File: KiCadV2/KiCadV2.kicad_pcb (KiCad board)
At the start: 2 copper layers, 76.4 x 51.6 mm, 148 parts, among them J1 USB_C_Receptacle_PowerOnly_6P, J3 Screw_Terminal_01x02, J4 Screw_Terminal_01x02, U1 MT3608, U10 NC7SZ157P6X, U11 NC7SZ157P6X, U12 NC7SZ157P6X, U13 NC7SZ157P6X, U14 74LV08AT14-13, U15 HIP4080A, U16 NC7SZ157P6X, U17 MX3502S, U18 MX3502S, U2 74HC595, U22 DMHT10H032LFJ, U23 INA240A1D, U26 MX3502S, U3 NC7SZ157P6X, U30 DMHT10H032LFJ, U31 INA240A1D, U32 NC7SZ157P6X, U33 NC7SZ157P6X, U34 NC7SZ157P6X, U35 NC7SZ157P6X, U36 NC7SZ157P6X, U37 NC7SZ157P6X, U38 74LV08AT14-13, U39 HIP4080A, U4 NC7SZ157P6X, U40 MCP6002-xSN, U41 CJ432, U5 MX3502S, U6 NC7SZ157P6X, U7 DAC082S085CISDX/NOPB, U8 NC7SZ157P6X, U9 NC7SZ157P6X

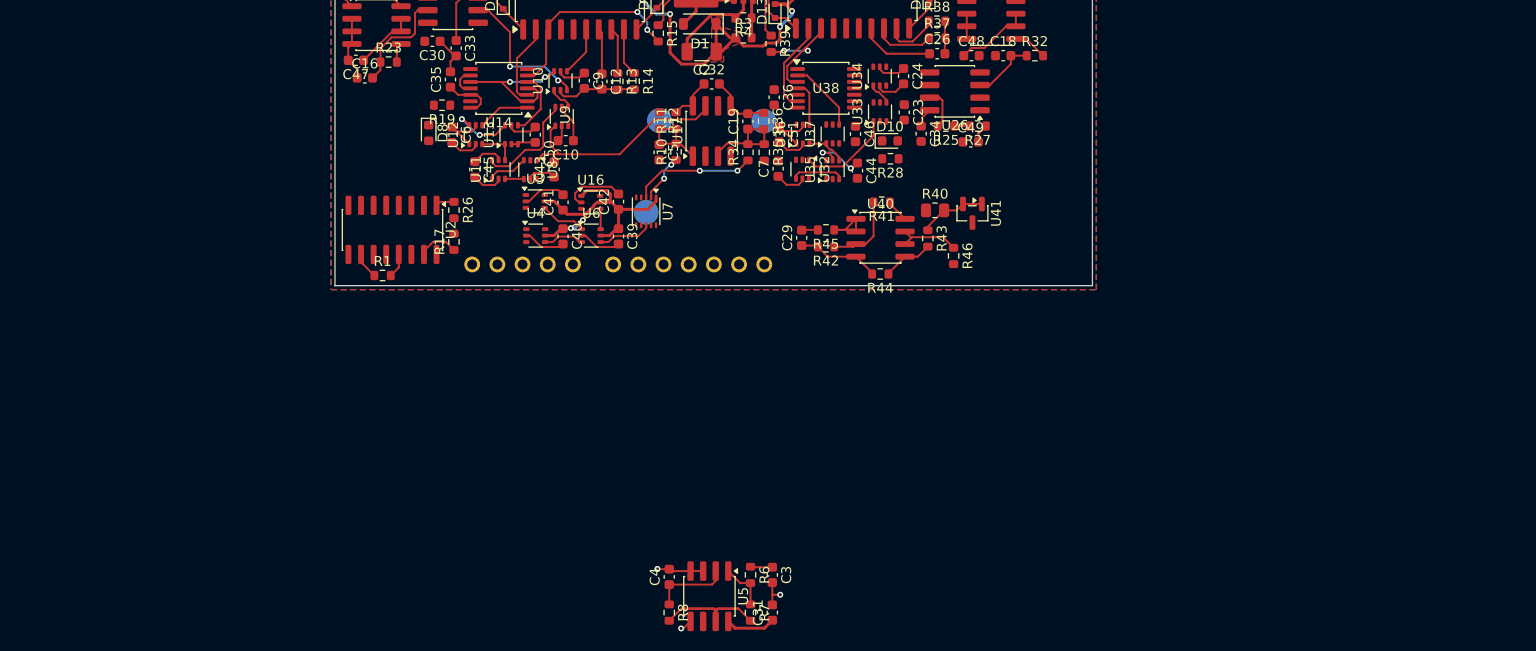
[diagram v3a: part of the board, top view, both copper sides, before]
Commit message: HF PWM done for both coils
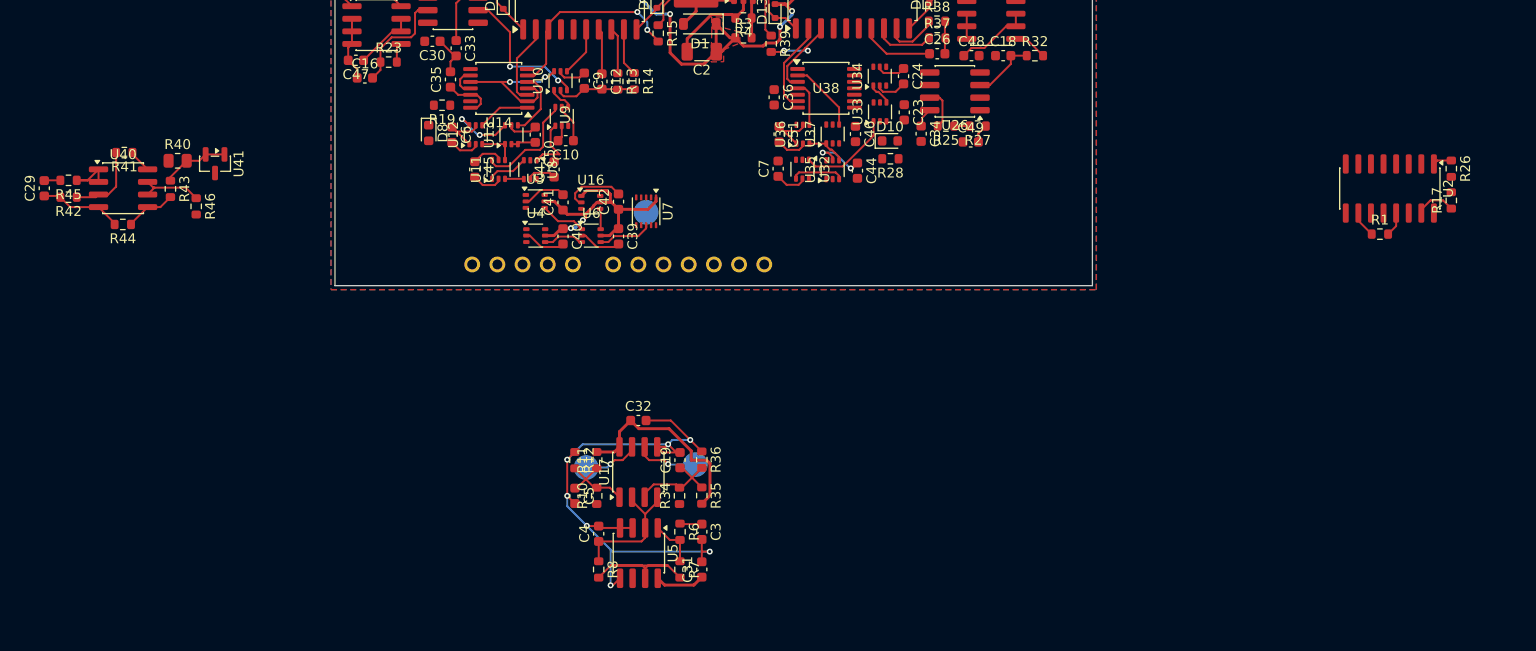
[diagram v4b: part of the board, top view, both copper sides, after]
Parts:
- moved R17 100.7 mm to (170.4, 165.6)
- moved R26 100.7 mm to (170.4, 162.4)
- moved R1 100.7 mm to (163.2, 169.0)
- moved U2 100.7 mm to (164.2, 164.4)
- moved C29 76.6 mm to (28.5, 164.4)
- moved R40 76.6 mm to (41.9, 161.6)
- moved R41 76.6 mm to (36.5, 160.8)
- moved R42 76.6 mm to (30.9, 165.3)
- moved R44 76.6 mm to (36.4, 168.0)
- moved R45 76.6 mm to (30.9, 163.6)
- moved R46 76.6 mm to (43.8, 166.2)
- moved U40 76.6 mm to (36.4, 164.4)
- moved R43 76.6 mm to (41.2, 164.4)
- moved U41 76.6 mm to (45.7, 161.9)
- moved TP2 35.8 mm to (83.1, 192.5)
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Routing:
- net GND: track 93.3 -> 139.2 mm, vias 3 -> 7
- net +5V: track 104.9 -> 120.7 mm
- net /DACOUT2: track 12.4 -> 0.00 mm, vias 2 -> 0
- net /PerCoil/SignalProcessingChain/HF PWM: track 22.6 -> 11.7 mm, vias 0 -> 1
- net /PerCoil1/SignalProcessingChain/HF PWM: track 9.54 -> 15.9 mm, vias 0 -> 1
- net /Vtri: track 7.83 -> 13.7 mm
- net /DACOUT1: track 4.89 -> 0.00 mm, vias 2 -> 0
- net Net-(U17B-+): track 9.52 -> 10.5 mm

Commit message: Hoo man
Right side coil type shit
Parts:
- moved U2 54.2 mm to (110.2, 169.2)
- moved R17 53.7 mm to (116.8, 168.8)
- moved R26 53.7 mm to (116.8, 165.2)
- moved R1 45.7 mm to (117.6, 172.0)
- moved C19 35.4 mm to (100.3, 157.3)
- moved C31 35.4 mm to (102.5, 168.3)
- moved C32 35.4 mm to (96.1, 153.3)
- moved R11 35.4 mm to (91.9, 157.3)
- moved R12 35.4 mm to (89.7, 157.3)
- moved R7 35.4 mm to (100.3, 168.3)
- moved R8 35.4 mm to (92.1, 168.3)
- moved U5 35.4 mm to (96.1, 166.6)
- moved C3 35.4 mm to (102.5, 164.5)
- moved C4 35.4 mm to (92.1, 164.7)
- moved C5 35.4 mm to (89.7, 160.9)
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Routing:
- net +5V: track 120.7 -> 171.1 mm, vias 4 -> 9
- net GND: track 139.2 -> 111.6 mm, vias 7 -> 6
- net /PerCoil1/OC_SENSE: track 7.73 -> 32.3 mm, vias 0 -> 2
- net /PerCoil1/~{OC1}: track 4.17 -> 21.3 mm, vias 0 -> 2
- net /PerCoil1/SignalProcessingChain/EN: track 0.00 -> 16.3 mm
- net /PerCoil1/SignalProcessingChain/HF PWM: track 15.9 -> 30.6 mm, vias 1 -> 3
- net /PerCoil1/SignalProcessingChain/DIR: track 0.00 -> 9.08 mm
- net /Analog2: track 6.43 -> 15.4 mm
- net /PerCoil1/SignalProcessingChain/Current_Dir: track 0.00 -> 7.88 mm
- net /D1: track 2.46 -> 9.00 mm
- net /PWM4: track 0.00 -> 5.78 mm, vias 0 -> 2
- net /EN1: track 3.75 -> 8.33 mm
- net /-OUT2: track 16.3 -> 20.2 mm
- net Net-(U26A-+): track 1.52 -> 4.31 mm
- net Net-(U39-LDEL): track 5.49 -> 7.54 mm
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
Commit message: Bunchhh of shit
PCB looking gooood
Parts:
- moved C29 35.6 mm to (62.9, 155.3), turned to 0 degrees
- moved R45 33.5 mm to (63.9, 158.2), turned to 90 degrees
- moved R42 31.6 mm to (61.7, 158.1), turned to 90 degrees
- moved R41 31.2 mm to (67.3, 166.3), turned to 90 degrees
- moved U40 26.9 mm to (63.3, 163.9), turned to -90 degrees
- moved R40 25.2 mm to (65.7, 170.1), turned to -90 degrees
- moved U41 25.0 mm to (69.3, 170.1), turned to 0 degrees
- moved R44 23.0 mm to (59.3, 165.7), turned to 90 degrees
- moved R43 21.8 mm to (62.5, 168.9), turned to 180 degrees
- moved R46 18.2 mm to (61.3, 171.0), turned to 180 degrees
- moved D8 0.21 mm to (67.2, 159.0), turned to 90 degrees
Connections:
- A1 pad 18: /PWM6 -> /PWM2
- A1 pad 20: /PWM5 -> /PWM1
- A1 pad 25: /PWM2 -> /PWM6
- A1 pad 26: /PWM1 -> /PWM5
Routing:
- net +5V: track 171.1 -> 348.0 mm, vias 9 -> 18
- net /D1: track 9.00 -> 47.9 mm
- net /D2: track 0.00 -> 33.3 mm, vias 0 -> 1
- net /D3: track 0.00 -> 25.9 mm
- net /PWM5: track 0.00 -> 21.4 mm
- net /PWM2: track 4.12 -> 19.4 mm, vias 0 -> 2
- net /PerCoil/SignalProcessingChain/HF PWM: track 11.7 -> 26.5 mm
- net /PWM3: track 0.00 -> 12.2 mm
- net Net-(D8-K): track 0.00 -> 6.56 mm
- net /PWM1: track 0.00 -> 6.51 mm
- net /PWM4: track 5.78 -> 11.5 mm
- net GND: track 111.6 -> 106.2 mm, vias 6 -> 25
- net /PWM6: track 0.00 -> 4.48 mm
- net Net-(D8-A): track 0.00 -> 3.14 mm
- net Net-(U40A--): track 5.97 -> 3.75 mm
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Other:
- board size 76.4 x 51.6 mm -> 76.4 x 52 mm

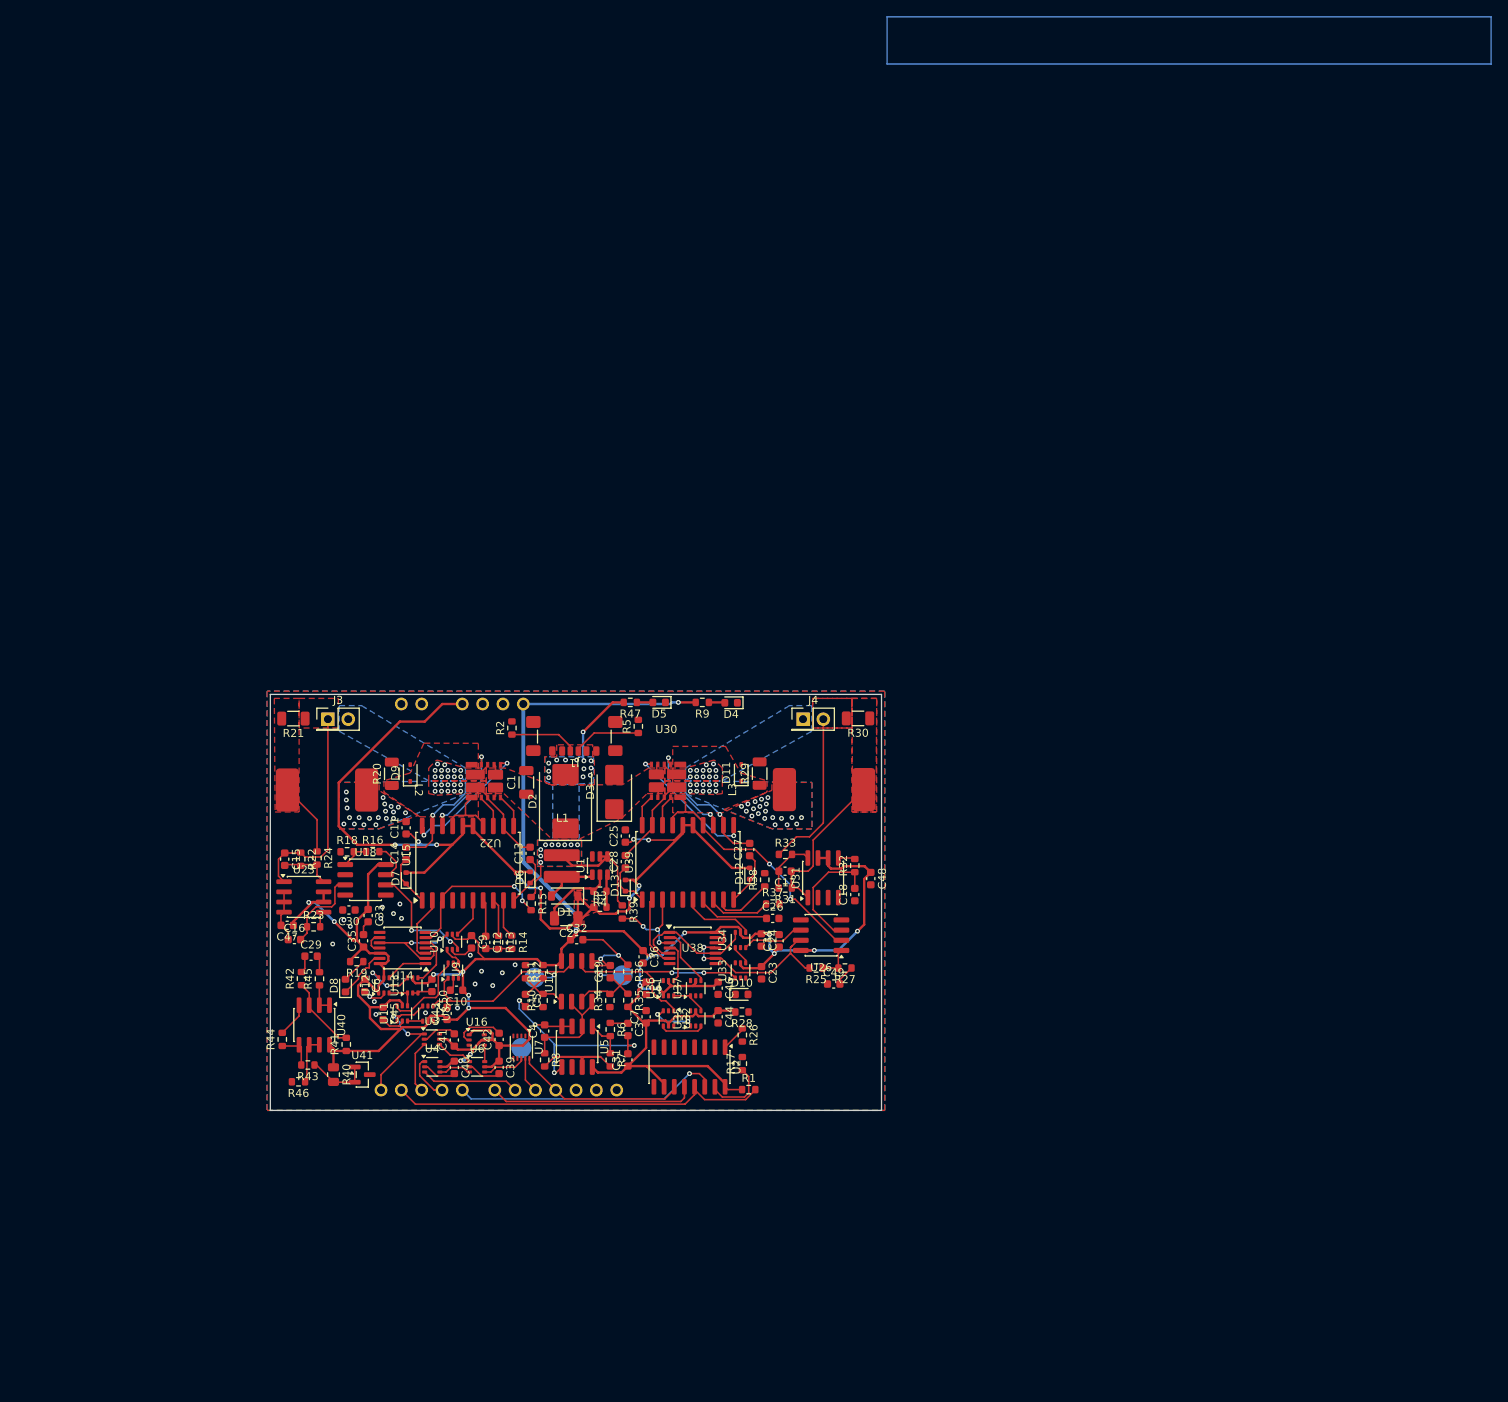
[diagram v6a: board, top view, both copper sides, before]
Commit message: Only GND via stitching left!!!
OMG OMG OMG PLEASE NO HUGE ERRORS
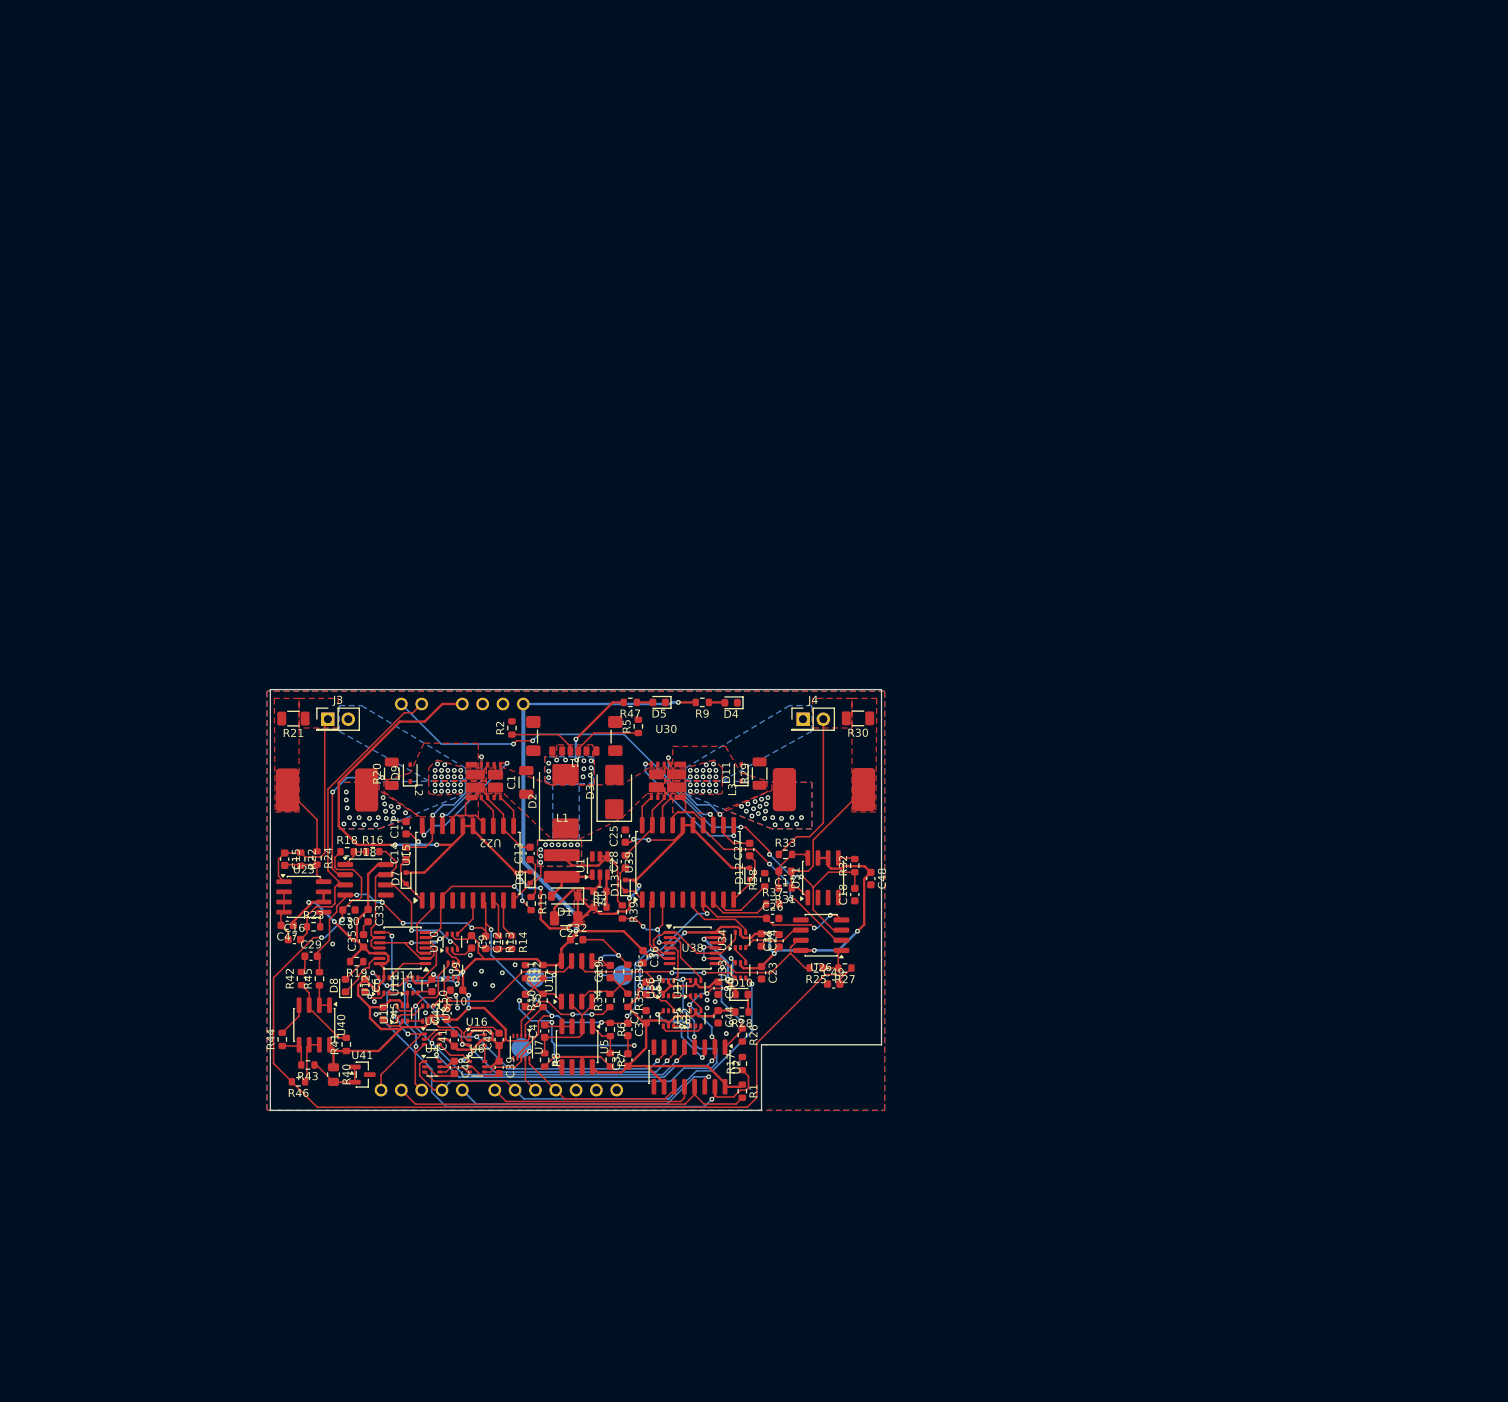
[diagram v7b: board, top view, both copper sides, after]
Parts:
- moved R1 0.82 mm to (116.8, 172.2), turned to -90 degrees
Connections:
- U2 pad 2: /A1 -> /A2
- U2 pad 3: /B1 -> /B2
- U2 pad 4: /C1 -> /C2
- U2 pad 5: /A2 -> /A1
- U2 pad 6: /B2 -> /B1
- U2 pad 7: /C2 -> /C1
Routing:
- net /0.2V: track 2.60 -> 122.5 mm, vias 0 -> 2
- net /VCM: track 18.1 -> 109.8 mm, vias 0 -> 11
- net /Analog2: track 15.4 -> 78.0 mm, vias 0 -> 5
- net /EN1: track 8.33 -> 70.0 mm, vias 0 -> 2
- net /A2: track 0.00 -> 57.2 mm, vias 0 -> 7
- net /PWM4: track 11.5 -> 55.2 mm
- net /A1: track 10.9 -> 53.1 mm, vias 0 -> 3
- net /PWM3: track 12.2 -> 52.8 mm, vias 0 -> 1
- net /C1: track 6.43 -> 46.3 mm, vias 2 -> 5
- net /B1: track 0.00 -> 37.3 mm, vias 0 -> 2
- net /Analog1: track 10.9 -> 40.1 mm
- net /PerCoil/OC_SENSE: track 7.90 -> 28.0 mm, vias 0 -> 2
- net /PWM1: track 6.51 -> 23.5 mm, vias 0 -> 2
- net /DACOUT2: track 0.00 -> 15.1 mm, vias 0 -> 2
- net /C2: track 0.00 -> 13.9 mm, vias 0 -> 3
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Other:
- board size 76.4 x 52 mm -> 76.4 x 52.6 mm

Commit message: Final version before trying JLCPCB
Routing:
- net GND: track 104.5 -> 106.2 mm, vias 27 -> 253
- net /PWM3: track 52.8 -> 54.0 mm, vias 1 -> 2
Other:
- board text added: "1+ 1-"
- board text added: "2+ 2-"
- board text added: "Arduino"
- board text added: "CAUTION!"
- board text added: "CAUTION! HOT!"
- board text added: "HOT!"
- board text added: "OC1"
- board text added: "OC2"
- board text added: "USB"
- board text added: "https://github.com/asdfgasdfgasdfg/Coil_driver"
- board text added: "{dblquote}Great discoveries begin with curiosity.{dblquote}"
